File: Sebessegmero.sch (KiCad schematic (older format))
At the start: 30 parts, among them J1 Conn_01x02_Female, J2 Conn_01x02_Female, J3 Screw_Terminal_01x02, J4 Conn_02x04_Odd_Even, J5 Conn_01x03_Female, U1 Opamp_Quad_Generic

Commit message: footprintek
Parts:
- A1: footprint (none) -> Footprints:MODULE_A000005
- J1, J2: footprint Connector_JST:JST_XH_B2B-XH-A_1x02_P2.50mm_Vertical -> Footprints:JST_B2B-XH-A(LF)(SN)
- J3: footprint (none) -> Footprints:TE_282837-2
- J4: footprint Connector_PinHeader_2.54mm:PinHeader_2x04_P2.54mm_Vertical_SMD -> Footprints:87758-0816
- J5: footprint Connector_JST:JST_XH_B3B-XH-A_1x03_P2.50mm_Vertical -> Footprints:JST_B3B-XH-A(LF)(SN)
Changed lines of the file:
@@
 F 0 "A1" H 2900 4061 50  0000 C CNN
 F 1 "Arduino_Nano_Every" H 2900 3970 50  0000 C CNN
-F 2 "" H 2900 5150 50  0001 C CIN
+F 2 "Footprints:MODULE_A000005" H 2900 5150 50  0001 C CIN
 F 3 "https://content.arduino.cc/assets/NANOEveryV3.0_sch.pdf" H 2900 5150 50  0001 C CNN
 	1    2900 5150
@@
 F 0 "J3" V 7214 712 50  0000 R CNN
 F 1 "Screw_Terminal_01x02" V 7123 712 50  0000 R CNN
-F 2 "" H 7250 900 50  0001 C CNN
+F 2 "Footprints:TE_282837-2" H 7250 900 50  0001 C CNN
 F 3 "https://hu.farnell.com/buchanan-te-connectivity/282837-2/terminal-block-pcb-2-position/dp/1784860?st=282837-2" H 7250 900 50  0001 C CNN
 	1    7250 900
@@
 F 0 "J4" H 9350 2467 50  0000 C CNN
 F 1 "Conn_02x04_Odd_Even" H 9350 2376 50  0000 C CNN
-F 2 "Connector_PinHeader_2.54mm:PinHeader_2x04_P2.54mm_Vertical_SMD" H 9300 2150 50  0001 C CNN
+F 2 "Footprints:87758-0816" H 9300 2150 50  0001 C CNN
 F 3 "https://hu.farnell.com/molex/87758-0816/connector-header-8pos-2row-2mm/dp/7472331" H 9300 2150 50  0001 C CNN
 	1    9300 2150
@@
 F 0 "J2" H 9942 1825 50  0000 C CNN
 F 1 "Conn_01x02_Female" H 9942 1916 50  0000 C CNN
-F 2 "Connector_JST:JST_XH_B2B-XH-A_1x02_P2.50mm_Vertical" H 10050 2150 50  0001 C CNN
+F 2 "Footprints:JST_B2B-XH-A(LF)(SN)" H 10050 2150 50  0001 C CNN
 F 3 "https://www.digikey.hu/product-detail/en/jst-sales-america-inc/B2B-XH-A-LF-SN/455-2247-ND/1651045" H 10050 2150 50  0001 C CNN
 	1    10050 2150
@@
 F 0 "J5" H 3928 5676 50  0000 L CNN
 F 1 "Conn_01x03_Female" H 3928 5585 50  0000 L CNN
-F 2 "Connector_JST:JST_XH_B3B-XH-A_1x03_P2.50mm_Vertical" H 3900 5650 50  0001 C CNN
+F 2 "Footprints:JST_B3B-XH-A(LF)(SN)" H 3900 5650 50  0001 C CNN
 F 3 "https://www.digikey.hu/product-detail/en/jst-sales-america-inc/B3B-XH-A-LF-SN/455-2248-ND/1651046" H 3900 5650 50  0001 C CNN
 	1    3900 5650
@@
 F 0 "J1" H 742 2675 50  0000 C CNN
 F 1 "Conn_01x02_Female" H 742 2766 50  0000 C CNN
-F 2 "Connector_JST:JST_XH_B2B-XH-A_1x02_P2.50mm_Vertical" H 850 3000 50  0001 C CNN
+F 2 "Footprints:JST_B2B-XH-A(LF)(SN)" H 850 3000 50  0001 C CNN
 F 3 "https://www.digikey.hu/product-detail/en/jst-sales-america-inc/B2B-XH-A-LF-SN/455-2247-ND/1651045" H 850 3000 50  0001 C CNN
 	1    850  3000

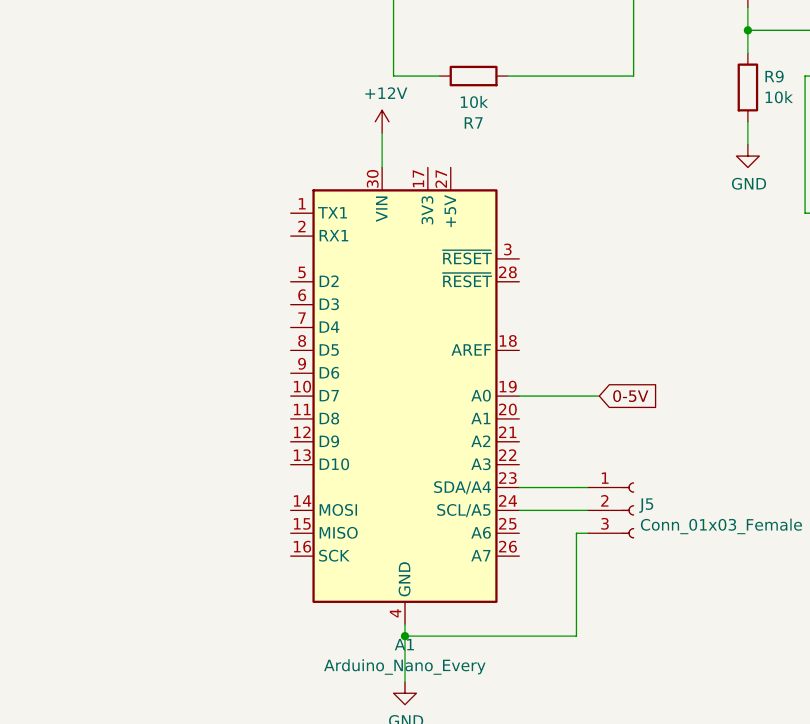
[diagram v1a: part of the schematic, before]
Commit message: footprint_elotti
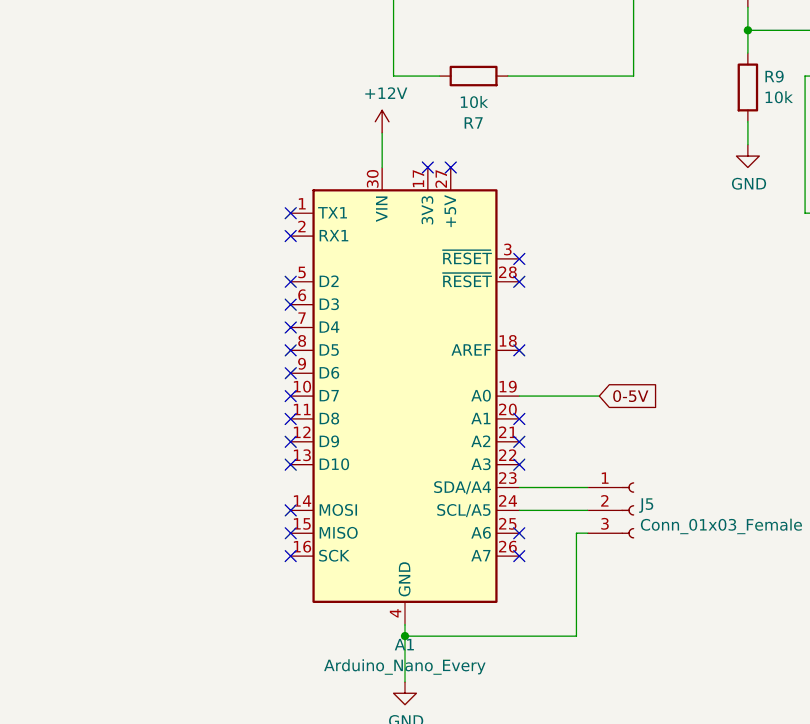
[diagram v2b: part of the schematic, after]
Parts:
- A1: footprint Footprints:MODULE_A000005 -> Module:Arduino_Nano
- J1, J2: footprint Footprints:JST_B2B-XH-A(LF)(SN) -> Connector_JST:JST_XH_B2B-XH-A_1x02_P2.50mm_Vertical
- J3: footprint Footprints:TE_282837-2 -> TerminalBlock_Phoenix:TerminalBlock_Phoenix_MKDS-1,5-2_1x02_P5.00mm_Horizontal
- J4: footprint Footprints:87758-0816 -> Connector_PinHeader_2.54mm:PinHeader_2x04_P2.54mm_Vertical
- J5: footprint Footprints:JST_B3B-XH-A(LF)(SN) -> Connector_JST:JST_XH_B3B-XH-A_1x03_P2.50mm_Vertical
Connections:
- no-connect marks 0 -> 24
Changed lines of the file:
@@
 F 0 "A1" H 2900 4061 50  0000 C CNN
 F 1 "Arduino_Nano_Every" H 2900 3970 50  0000 C CNN
-F 2 "Footprints:MODULE_A000005" H 2900 5150 50  0001 C CIN
+F 2 "Module:Arduino_Nano" H 2900 5150 50  0001 C CIN
 F 3 "https://content.arduino.cc/assets/NANOEveryV3.0_sch.pdf" H 2900 5150 50  0001 C CNN
 	1    2900 5150
@@
 F 0 "J3" V 7214 712 50  0000 R CNN
 F 1 "Screw_Terminal_01x02" V 7123 712 50  0000 R CNN
-F 2 "Footprints:TE_282837-2" H 7250 900 50  0001 C CNN
+F 2 "TerminalBlock_Phoenix:TerminalBlock_Phoenix_MKDS-1,5-2_1x02_P5.00mm_Horizontal" H 7250 900 50  0001 C CNN
 F 3 "https://hu.farnell.com/buchanan-te-connectivity/282837-2/terminal-block-pcb-2-position/dp/1784860?st=282837-2" H 7250 900 50  0001 C CNN
 	1    7250 900
@@
 F 0 "J4" H 9350 2467 50  0000 C CNN
 F 1 "Conn_02x04_Odd_Even" H 9350 2376 50  0000 C CNN
-F 2 "Footprints:87758-0816" H 9300 2150 50  0001 C CNN
+F 2 "Connector_PinHeader_2.54mm:PinHeader_2x04_P2.54mm_Vertical" H 9300 2150 50  0001 C CNN
 F 3 "https://hu.farnell.com/molex/87758-0816/connector-header-8pos-2row-2mm/dp/7472331" H 9300 2150 50  0001 C CNN
 	1    9300 2150
@@
 F 0 "J2" H 9942 1825 50  0000 C CNN
 F 1 "Conn_01x02_Female" H 9942 1916 50  0000 C CNN
-F 2 "Footprints:JST_B2B-XH-A(LF)(SN)" H 10050 2150 50  0001 C CNN
+F 2 "Connector_JST:JST_XH_B2B-XH-A_1x02_P2.50mm_Vertical" H 10050 2150 50  0001 C CNN
 F 3 "https://www.digikey.hu/product-detail/en/jst-sales-america-inc/B2B-XH-A-LF-SN/455-2247-ND/1651045" H 10050 2150 50  0001 C CNN
 	1    10050 2150
@@
 F 0 "J5" H 3928 5676 50  0000 L CNN
 F 1 "Conn_01x03_Female" H 3928 5585 50  0000 L CNN
-F 2 "Footprints:JST_B3B-XH-A(LF)(SN)" H 3900 5650 50  0001 C CNN
+F 2 "Connector_JST:JST_XH_B3B-XH-A_1x03_P2.50mm_Vertical" H 3900 5650 50  0001 C CNN
 F 3 "https://www.digikey.hu/product-detail/en/jst-sales-america-inc/B3B-XH-A-LF-SN/455-2248-ND/1651046" H 3900 5650 50  0001 C CNN
 	1    3900 5650
@@
 F 0 "J1" H 742 2675 50  0000 C CNN
 F 1 "Conn_01x02_Female" H 742 2766 50  0000 C CNN
-F 2 "Footprints:JST_B2B-XH-A(LF)(SN)" H 850 3000 50  0001 C CNN
+F 2 "Connector_JST:JST_XH_B2B-XH-A_1x02_P2.50mm_Vertical" H 850 3000 50  0001 C CNN
 F 3 "https://www.digikey.hu/product-detail/en/jst-sales-america-inc/B2B-XH-A-LF-SN/455-2247-ND/1651045" H 850 3000 50  0001 C CNN
 	1    850  3000
@@
 Wire Wire Line
 	1200 3150 1750 3150
+NoConn ~ 3400 4950
+NoConn ~ 3400 4650
+NoConn ~ 3400 4550
+NoConn ~ 3100 4150
+NoConn ~ 3000 4150
+NoConn ~ 2400 4350
+NoConn ~ 2400 4450
+NoConn ~ 2400 4650
+NoConn ~ 2400 4750
+NoConn ~ 2400 4850
+NoConn ~ 2400 4950
+NoConn ~ 2400 5050
+NoConn ~ 2400 5150
+NoConn ~ 2400 5250
+NoConn ~ 2400 5350
+NoConn ~ 2400 5450
+NoConn ~ 2400 5650
+NoConn ~ 2400 5750
+NoConn ~ 2400 5850
+NoConn ~ 3400 5850
+NoConn ~ 3400 5750
+NoConn ~ 3400 5450
+NoConn ~ 3400 5350
+NoConn ~ 3400 5250
 $EndSCHEMATC
